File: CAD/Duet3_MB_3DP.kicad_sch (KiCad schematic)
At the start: 0 parts

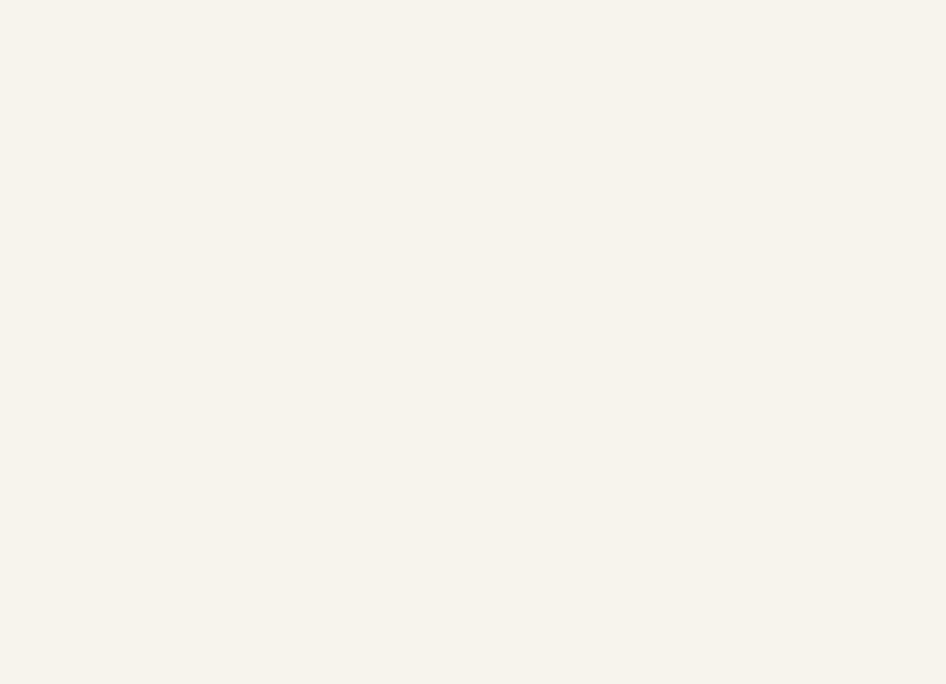
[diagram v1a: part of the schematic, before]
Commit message: Add PDN Directives
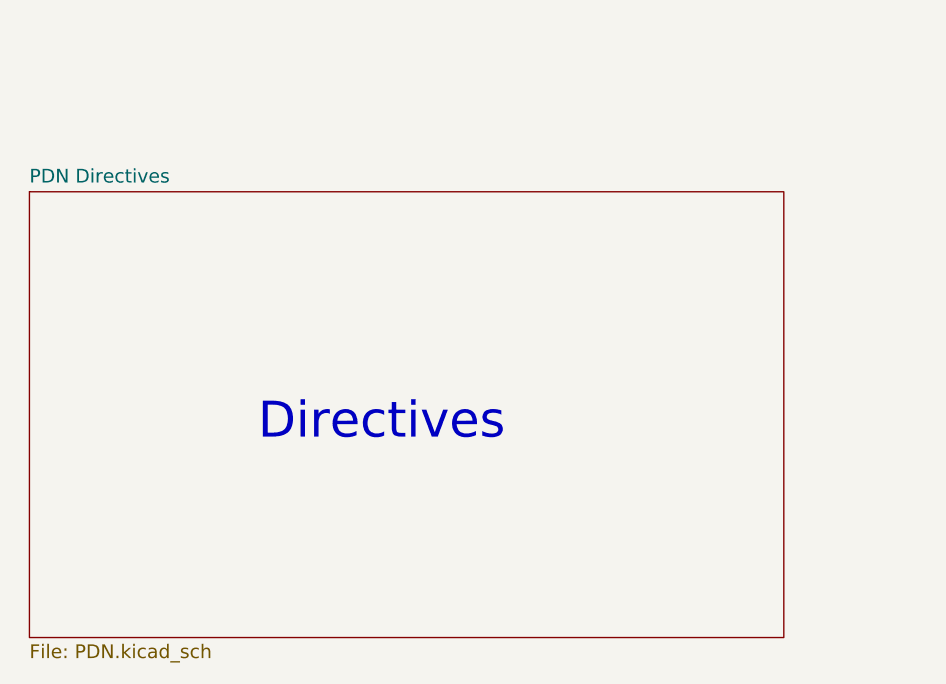
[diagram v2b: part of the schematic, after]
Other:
- added sheet PDN Directives (PDN.kicad_sch)
- note added: "Directives"
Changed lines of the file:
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@@
+		)
+	)
+	(text "Directives"
+		(exclude_from_sim no)
+		(at 41.91 382.27 0)
+		(effects
+			(font
+				(size 3.9878 3.9878)
+			)
+			(justify left bottom)
 		)
 	)
@@
 				)
 			)
+		)
+	)
+	(sheet
+		(at 16.51 354.33)
+		(size 83.82 49.53)
+		(exclude_from_sim no)
+		(in_bom yes)
+		(on_board yes)
+		(dnp no)
+		(fields_autoplaced yes)
+		(stroke
+			(width 0.1524)
+			(type solid)
+		)
+		(fill
+			(color 0 0 0 0)
+		)
+		(property "Sheetname" "PDN Directives"
+			(at 16.51 353.4914 0)
+			(show_name no)
+			(do_not_autoplace no)
+			(effects
+				(font
+					(size 1.524 1.524)
+				)
+				(justify left bottom)
+			)
+		)
+		(property "Sheetfile" "PDN.kicad_sch"
+			(at 16.51 404.5462 0)
+			(show_name no)
+			(do_not_autoplace no)
+			(effects
+				(font
+					(size 1.524 1.524)
+				)
+				(justify left top)
+			)
+		)
+		(instances
+			(project "Duet3_MB_3DP"
+				(path "/94813053-1316-4754-9fb4-4dbbf7dc780d"
+					(page "8")
+				)
+			)

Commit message: Part Alternatives
Changed some alternatives for certain parts as they are out of stock and some won't come in until March 27
Also changed C6 so it uses the same cap as C29 so that manufacturing costs are lower
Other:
- note added: "Part ordering info: Caps from Murata's GCM series or GRT series, do not GRM unless GCM and GRT not usable Resistors from YAGEO's AC series or AF series, do not RC unless AC and AF not usable"
- note added: "Quality (Higher)---> RC<AC<AF GRM<GRT<GCM"
- note removed: "Part ordering info: Caps from Murata's GCM series or GRT series Resistors from YAGEO's AC series or AT series"
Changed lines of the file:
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@@
 		)
 	)
-	(text "Part ordering info:\nCaps from Murata's GCM series or GRT series\nResistors from YAGEO's AC series or AT series"
+	(text "Part ordering info:\nCaps from Murata's GCM series or GRT series, do not GRM unless GCM and GRT not usable\nResistors from YAGEO's AC series or AF series, do not RC unless AC and AF not usable"
 		(exclude_from_sim no)
-		(at 101.346 153.162 0)
+		(at 49.276 215.392 0)
 		(effects
 			(font
@@
 		)
 	)
+	(text "Quality (Higher)--->\nRC<AC<AF\nGRM<GRT<GCM"
+		(exclude_from_sim no)
+		(at 133.35 233.68 0)
+		(effects
+			(font
+				(size 2.54 2.54)
+			)
+		)
+	)
